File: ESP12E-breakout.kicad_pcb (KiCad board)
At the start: 2 copper layers, 26.7 x 35.1 mm, 17 parts, among them P1 CONN_01X10, P3 CONN_01X08, SW1 RESET, SW2 FLASH, U1 ESP-12E, U2 AP1117

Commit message: Ready for prototype run
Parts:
- D1: value PWR -> LED
- SW1, SW2: footprint w_switch:PCB_PUSH_edit -> w_switch:smd_push
- moved C1 15.8 mm to (185.9, 70.9), turned to 0 degrees
- moved D1 9.17 mm to (183.6, 77.1)
- moved SW1 9.04 mm to (182.1, 67.8), turned to 180 degrees
- moved R6 8.87 mm to (183.4, 74.8)
- moved SW2 7.17 mm to (171.6, 67.8), turned to 0 degrees
- moved R5 6.32 mm to (173.0, 75.1)
- moved R4 6.19 mm to (173.0, 72.8)
- moved R3 6.07 mm to (173.0, 70.5), turned to 180 degrees
- moved R1 5.51 mm to (173.0, 66.0)
- moved R2 5.51 mm to (173.0, 68.2)
- moved G1 4.40 mm to (175.4, 75.2)
- moved C2 2.52 mm to (185.9, 73.2)
- moved U2 1.14 mm to (179.6, 72.6)
- renumbered G*** to G0, G*** to G1
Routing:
- net GND: track 82.4 -> 64.4 mm
- net /15: track 17.0 -> 26.5 mm
- net /2: track 16.8 -> 23.6 mm
- net /0: track 41.5 -> 35.1 mm
- net /3V3: track 50.9 -> 44.8 mm, vias 0 -> 2
- net /5V: track 24.3 -> 19.0 mm
- net /CH_PD: track 24.2 -> 27.5 mm
- net /RESET: track 60.3 -> 57.3 mm
- added copper zone on B.Cu, net /3V3
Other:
- outline, holes or cut-outs redrawn
- board text added: "Vin"
- board text removed: "MADE IN INDIA"
- board text removed: "V IN"

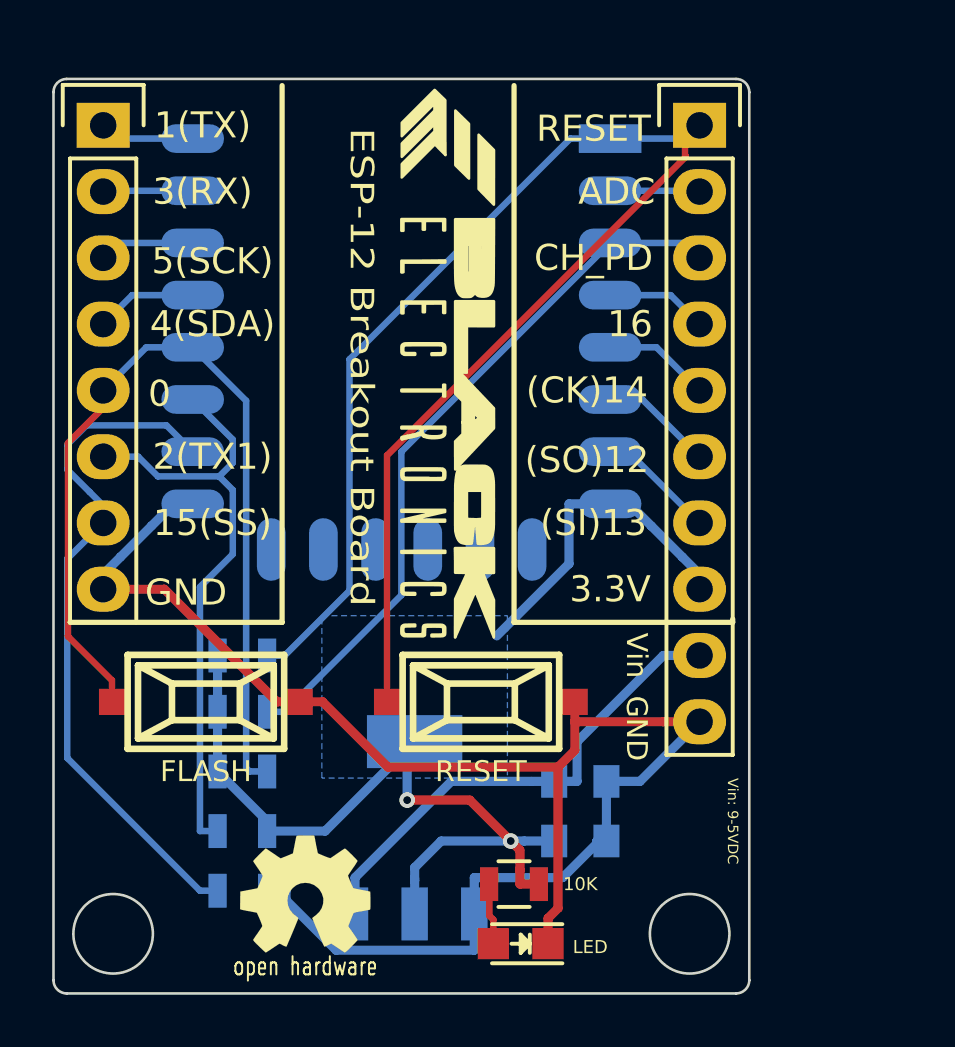
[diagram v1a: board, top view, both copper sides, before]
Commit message: removed vias
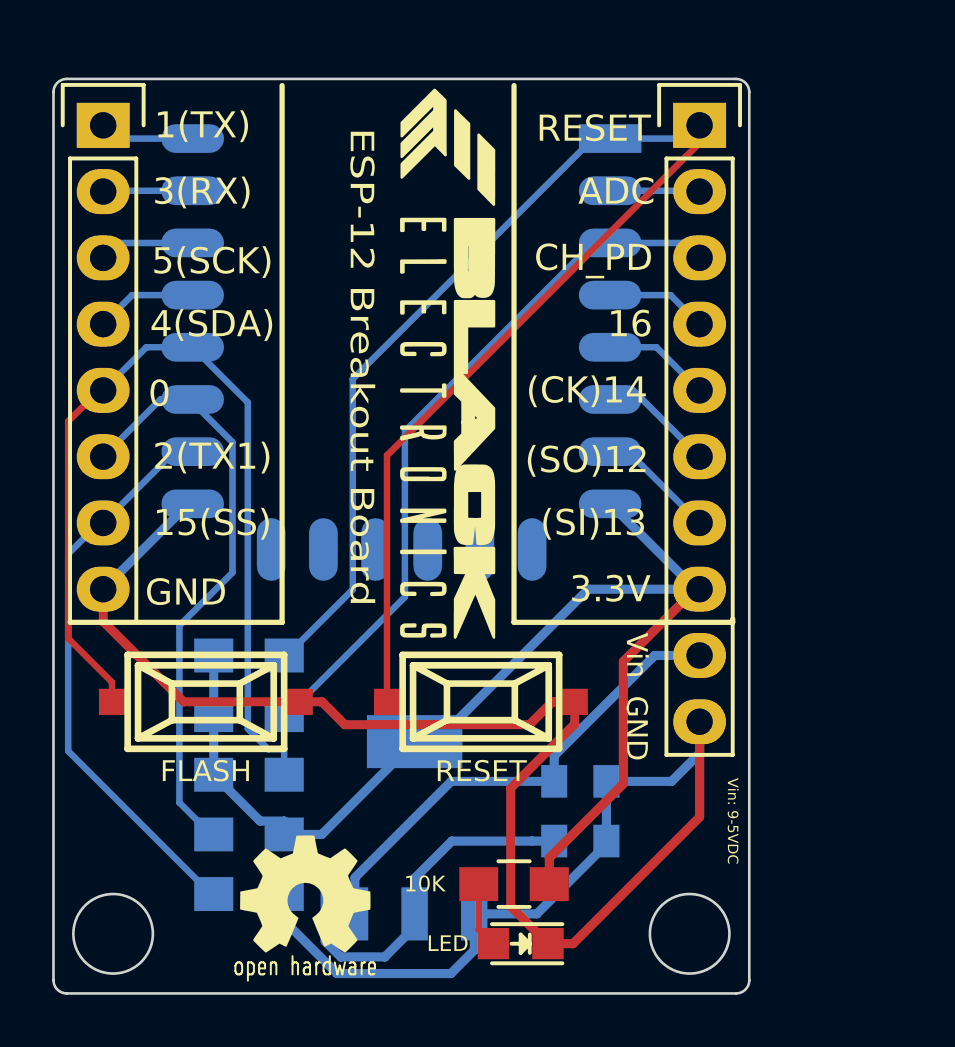
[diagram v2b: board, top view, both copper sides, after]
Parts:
- R1, R2, R3, R4, R5, R6: footprint Resistors_SMD:R_0805 -> Resistors_SMD:R_0805_HandSoldering
- moved R2 0.28 mm to (173.2, 68.3)
- moved R3 0.28 mm to (173.2, 70.6)
- moved R4 0.28 mm to (173.2, 72.9)
- moved R5 0.28 mm to (173.2, 75.2)
- moved R1 0.25 mm to (173.2, 66.0)
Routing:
- net /3V3: track 44.8 -> 64.2 mm, vias 2 -> 0
- net GND: track 64.4 -> 73.4 mm
- net /15: track 26.5 -> 21.8 mm
- net /RESET: track 57.3 -> 56.1 mm
- removed copper zone on B.Cu, net /3V3

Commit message: Sent for Fab
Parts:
- removed G0: LOGO, logo:3k5
- removed G1: LOGO, logo:oshw-logo-kicad-copper-10mm
- added P2: Logo, logo:3k5, F.Cu at (177.5, 56.5)
- added P4: OSHW logo, logo:oshw-logo-kicad-copper-10mm, F.Cu at (190.6, 67.6)
- P1, P3: moved to B.Cu
- U1: footprint ESP8266:ESP-12E -> ESP8266:ESP-12E_SilkOutline
- U2: value AP1117 -> 1117-3V3
- moved R5 25.7 mm to (196.2, 63.8), turned to 270 degrees
- moved D1 25.6 mm to (193.3, 53.3)
- moved R6 25.6 mm to (193.3, 51.2), turned to 180 degrees
- moved C2 24.8 mm to (197.0, 50.9), turned to 90 degrees
- moved P3 23.9 mm to (168.4, 69.6), turned to 270 degrees
- moved R4 22.7 mm to (194.1, 63.8), turned to 90 degrees
- moved SW2 22.4 mm to (193.2, 62.0), turned to 180 degrees
- moved U2 22.3 mm to (192.2, 54.2)
- moved P1 22.1 mm to (168.4, 46.7), turned to 270 degrees
- moved C1 20.0 mm to (187.3, 50.9), turned to 90 degrees
- moved R3 19.9 mm to (191.9, 63.8), turned to 270 degrees
- moved U1 18.6 mm to (168.9, 50.2), turned to 270 degrees
- moved R2 17.1 mm to (189.7, 63.8), turned to 270 degrees
- moved SW1 15.0 mm to (193.3, 57.8), turned to 0 degrees
- moved R1 14.5 mm to (187.6, 63.8), turned to 270 degrees
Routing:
- net GND: track 73.4 -> 86.2 mm
- net /0: track 35.6 -> 44.0 mm
- net /RESET: track 56.1 -> 61.5 mm
- net /5V: track 18.7 -> 16.1 mm
- net /15: track 21.8 -> 23.0 mm
- net /CH_PD: track 27.6 -> 26.5 mm
- net /2: track 23.1 -> 22.0 mm
- net /3V3: track 64.2 -> 65.3 mm
- net Net-(D1-Pad2): track 2.52 -> 3.29 mm
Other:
- board size 26.7 x 35.1 mm -> 31.6 x 26.7 mm
- board text added: "1117-3.3V"
- board text added: "Designed & Made in INDIA"
- board text added: "ESP-12 Dev Board"
- board text added: "Vin: 5-9VDC"
- board text removed: "ESP-12 Breakout Board"
- board text removed: "These pretzels are making me thirsty"
- board text removed: "Vin: 9-5VDC"
